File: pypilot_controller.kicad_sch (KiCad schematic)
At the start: 29 parts, among them J1 power+, J2 power-, J3 power+, J4 power+, Q1 Q_NMOS_GDS, Q2 Q_NMOS_GDS, Q3 Q_NMOS_GDS, Q4 Q_NMOS_GDS, Q5 Q_NMOS_GDS, U2 IR2101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

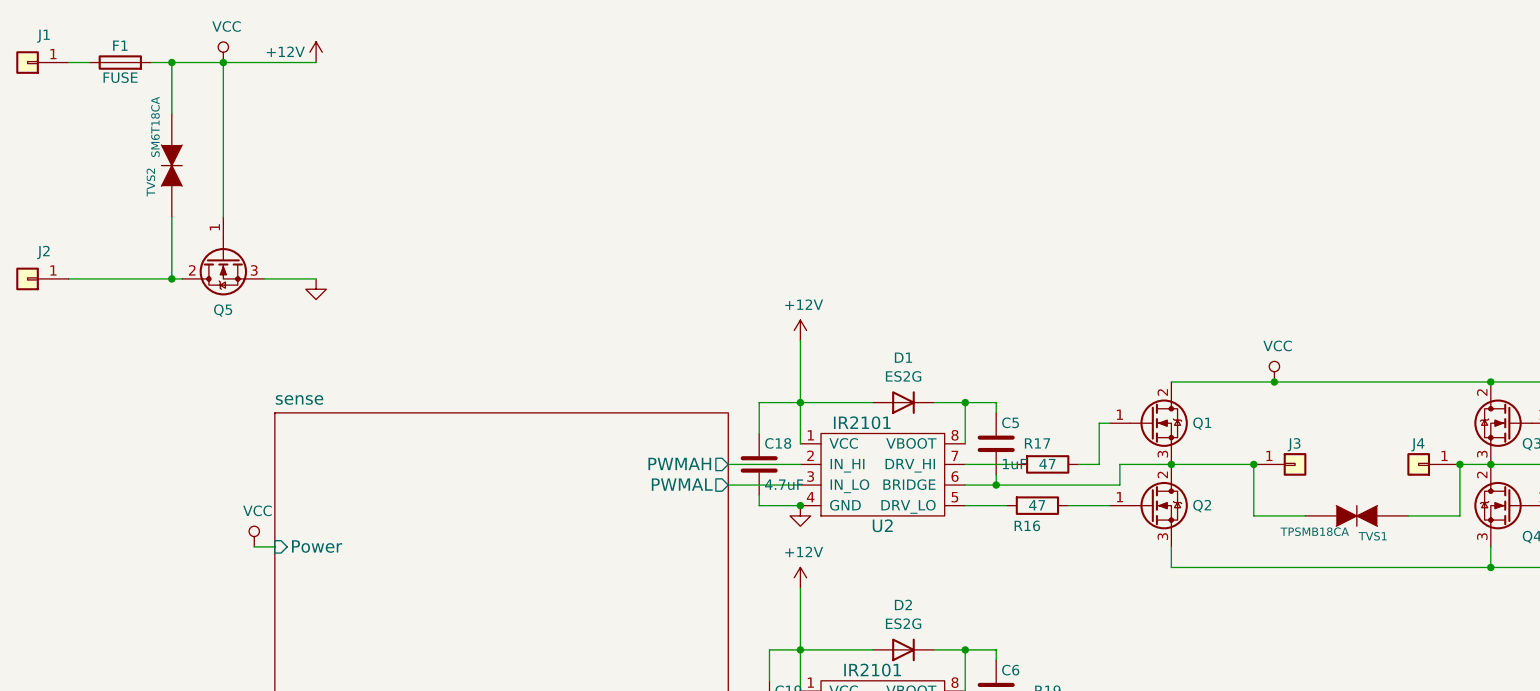
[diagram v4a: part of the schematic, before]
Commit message: Update every symbol in the schematic
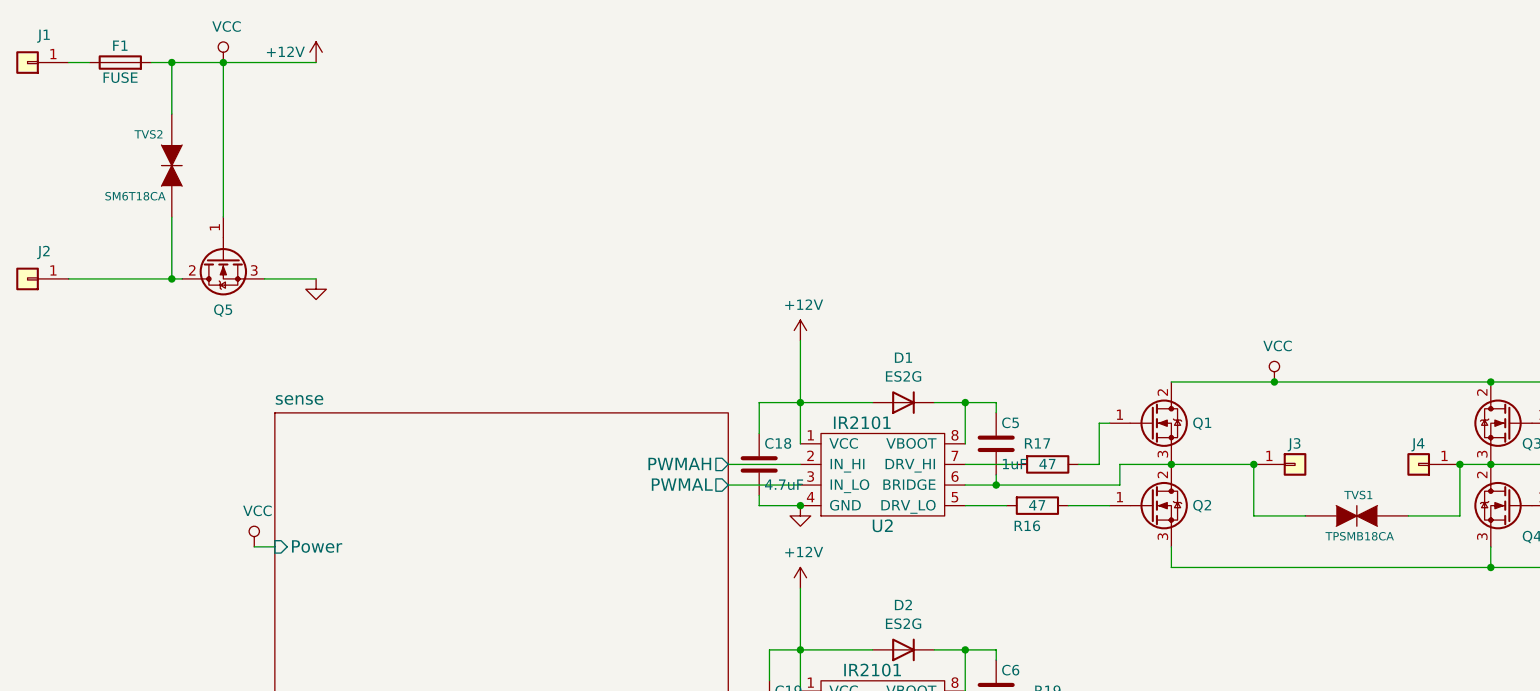
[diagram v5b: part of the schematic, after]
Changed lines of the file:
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@@
 			)
 		)
-		(property "Datasheet" ""
+		(property "Datasheet" "~"
 			(at 238.76 101.6 0)
 			(effects
@@
 			)
 		)
-		(property "Description" ""
+		(property "Description" "Resistor"
 			(at 238.76 101.6 0)
 			(effects
@@
 			)
 		)
-		(property "Datasheet" ""
+		(property "Datasheet" "~"
 			(at 215.9 85.09 0)
 			(effects
@@
 			)
 		)
-		(property "Description" ""
+		(property "Description" "N-MOSFET transistor, gate/drain/source"
 			(at 215.9 85.09 0)
 			(effects
@@
 			)
 		)
-		(property "Description" ""
+		(property "Description" "Power symbol creates a global label with name \"GND\" , ground"
 			(at 128.27 115.57 0)
 			(effects
@@
 			)
 		)
-		(property "Description" ""
+		(property "Description" "Power symbol creates a global label with name \"GND\" , ground"
 			(at 128.27 85.09 0)
 			(effects
@@
 			)
 		)
-		(property "Datasheet" ""
+		(property "Datasheet" "~"
 			(at 215.9 74.93 0)
 			(effects
@@
 			)
 		)
-		(property "Description" ""
+		(property "Description" "N-MOSFET transistor, gate/drain/source"
 			(at 215.9 74.93 0)
 			(effects
@@
 			)
 		)
-		(property "Datasheet" ""
+		(property "Datasheet" "~"
 			(at 171.45 74.93 0)
 			(effects
@@
 			)
 		)
-		(property "Description" ""
+		(property "Description" "N-MOSFET transistor, gate/drain/source"
 			(at 171.45 74.93 0)
 			(effects
@@
 			)
 		)
-		(property "Datasheet" ""
+		(property "Datasheet" "~"
 			(at 171.45 85.09 0)
 			(effects
@@
 			)
 		)
-		(property "Description" ""
+		(property "Description" "N-MOSFET transistor, gate/drain/source"
 			(at 171.45 85.09 0)
 			(effects
@@
 			)
 		)
-		(property "Description" ""
+		(property "Description" "Power symbol creates a global label with name \"GND\" , ground"
 			(at 238.76 106.68 0)
 			(effects
@@
 		)
 		(property "Footprint" "Resistor_SMD:R_0805_2012Metric"
+			(at 157.48 83.312 90)
+			(effects
+				(font
+					(size 1.27 1.27)
+				)
+				(hide yes)
+			)
+		)
+		(property "Datasheet" "~"
 			(at 157.48 85.09 0)
 			(effects
@@
 			)
 		)
-		(property "Datasheet" ""
-			(at 157.48 85.09 0)
-			(effects
-				(font
-					(size 1.27 1.27)
-				)
-				(hide yes)
-			)
-		)
-		(property "Description" ""
+		(property "Description" "Resistor"
 			(at 157.48 85.09 0)
 			(effects
@@
 		)
 		(property "Footprint" "Resistor_SMD:R_0805_2012Metric"
+			(at 158.75 78.232 90)
+			(effects
+				(font
+					(size 1.27 1.27)
+				)
+				(hide yes)
+			)
+		)
+		(property "Datasheet" "~"
 			(at 158.75 80.01 0)
 			(effects
@@
 			)
 		)
-		(property "Datasheet" ""
-			(at 158.75 80.01 0)
-			(effects
-				(font
-					(size 1.27 1.27)
-				)
-				(hide yes)
-			)
-		)
-		(property "Description" ""
+		(property "Description" "Resistor"
 			(at 158.75 80.01 0)
 			(effects
@@
 		)
 		(property "Footprint" "Resistor_SMD:R_0805_2012Metric"
+			(at 158.75 108.712 90)
+			(effects
+				(font
+					(size 1.27 1.27)
+				)
+				(hide yes)
+			)
+		)
+		(property "Datasheet" "~"
 			(at 158.75 110.49 0)
 			(effects
@@
 			)
 		)
-		(property "Datasheet" ""
-			(at 158.75 110.49 0)
-			(effects
-				(font
-					(size 1.27 1.27)
-				)
-				(hide yes)
-			)
-		)
-		(property "Description" ""
+		(property "Description" "Resistor"
 			(at 158.75 110.49 0)
 			(effects
@@
 		)
 		(property "Footprint" "Resistor_SMD:R_0805_2012Metric"
+			(at 157.48 113.792 90)
+			(effects
+				(font
+					(size 1.27 1.27)
+				)
+				(hide yes)
+			)
+		)
+		(property "Datasheet" "~"
 			(at 157.48 115.57 0)
 			(effects
@@
 			)
 		)
-		(property "Datasheet" ""
-			(at 157.48 115.57 0)
-			(effects
-				(font
-					(size 1.27 1.27)
-				)
-				(hide yes)
-			)
-		)
-		(property "Description" ""
+		(property "Description" "Resistor"
 			(at 157.48 115.57 0)
 			(effects
@@
 		(dnp no)
 		(property "Reference" "TVS1"
-			(at 200.66 88.9 0)
+			(at 198.882 83.82 0)
 			(effects
 				(font
@@
 		)
 		(property "Value" "TPSMB18CA"
-			(at 195.8848 88.3412 0)
+			(at 201.422 88.9 0)
 			(effects
 				(font
@@
 		)
 		(property "Footprint" "pypilot_controller_footprints:D_SMB_TVS"
-			(at 194.9196 88.3412 90)
+			(at 198.12 86.36 0)
 			(effects
 				(font
 					(size 1.524 1.524)
 				)
-				(justify left)
 				(hide yes)
 			)
@@
 			)
 		)
-		(property "Description" ""
+		(property "Description" "Power symbol creates a global label with name \"GND\" , ground"
 			(at 68.58 57.15 0)
 			(effects
@@
 			)
 		)
-		(property "Datasheet" "C67278"
+		(property "Datasheet" "~"
 			(at 57.15 54.61 0)
 			(effects
@@
 			)
 		)
-		(property "Description" ""
+		(property "Description" "N-MOSFET transistor, gate/drain/source"
 			(at 57.15 54.61 0)
 			(effects
@@
 			)
 		)
-		(property "Datasheet" "C487394"
+		(property "Datasheet" "~"
 			(at 229.87 80.01 0)
 			(effects
@@
 			)
 		)
-		(property "Datasheet" "C487394"
+		(property "Datasheet" "~"
 			(at 234.95 86.36 0)
 			(effects
@@
 		(dnp no)
 		(property "Reference" "TVS2"
-			(at 48.26 46.99 0)
+			(at 49.784 39.37 90)
 			(effects
 				(font
@@
 		)
 		(property "Value" "SM6T18CA"
-			(at 48.8188 42.2148 0)
+			(at 50.038 46.99 90)
 			(effects
 				(font
@@
 		)
 		(property "Footprint" "pypilot_controller_footprints:D_SMB_TVS"
-			(at 48.8188 41.2496 90)
+			(at 50.8 44.45 0)
 			(effects
 				(font
 					(size 1.524 1.524)
 				)
-				(justify left)
 				(hide yes)
 			)
@@
 			)
 		)
-		(property "Description" ""
+		(property "Description" "Power symbol creates a global label with name \"+12V\""
 			(at 128.27 95.25 0)
 			(effects
@@
 			)
 		)
-		(property "Description" ""
+		(property "Description" "Power symbol creates a global label with name \"+12V\""
 			(at 128.27 64.77 0)
 			(effects
@@
 			)
 		)
-		(property "Description" ""
+		(property "Description" "Power symbol creates a global label with name \"+12V\""
 			(at 68.58 30.48 0)
 			(effects
@@
 			)
 		)
-		(property "Datasheet" "C2935871, C668119, C3204137"
+		(property "Datasheet" "~"
 			(at 44.45 30.48 0)
 			(effects
@@
 			)
 		)
-		(property "Description" ""
+		(property "Description" "Generic connector, single row, 01x01, script generated (kicad-library-utils/schlib/autogen/connector/)"
 			(at 33.02 57.15 0)
 			(effects
@@
 			)
 		)
-		(property "Description" ""
+		(property "Description" "Generic connector, single row, 01x01, script generated (kicad-library-utils/schlib/autogen/connector/)"
 			(at 33.02 30.48 0)
 			(effects
@@
 			)
 		)
-		(property "Description" ""
+		(property "Description" "Generic connector, single row, 01x01, script generated (kicad-library-utils/schlib/autogen/connector/)"
 			(at 189.23 80.01 0)
 			(effects
@@
 			)
 		)
-		(property "Description" ""
+		(property "Description" "Generic connector, single row, 01x01, script generated (kicad-library-utils/schlib/autogen/connector/)"
 			(at 204.47 80.01 0)
 			(effects

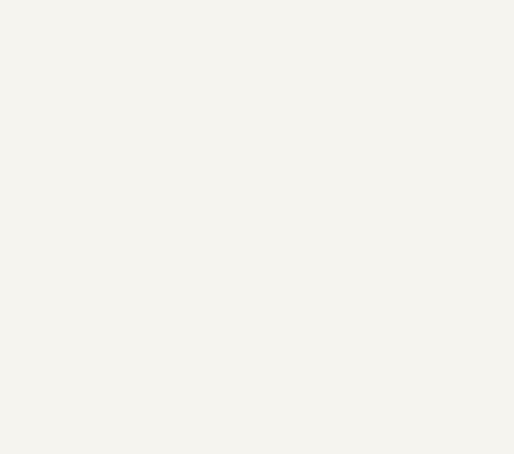
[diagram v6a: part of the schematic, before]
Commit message: Added symbols for mounting and cable tie holes, to avoid warning on import from schematic
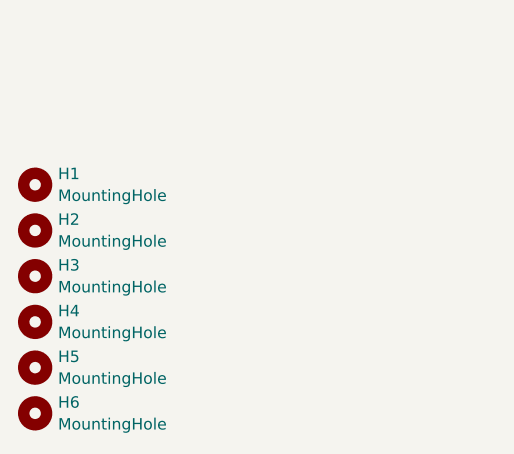
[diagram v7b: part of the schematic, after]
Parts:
- added H1, H2, H3, H4: MountingHole, MountingHole:MountingHole_3.2mm_M3, symbol Mechanical:MountingHole
- added H5, H6: MountingHole, MountingHole:MountingHole_2.5mm, symbol Mechanical:MountingHole
